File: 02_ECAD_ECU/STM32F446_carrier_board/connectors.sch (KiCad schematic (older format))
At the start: 2 parts, among them J1 FX10A-168S-SV, J2 FX10A-168P-SV_(71)

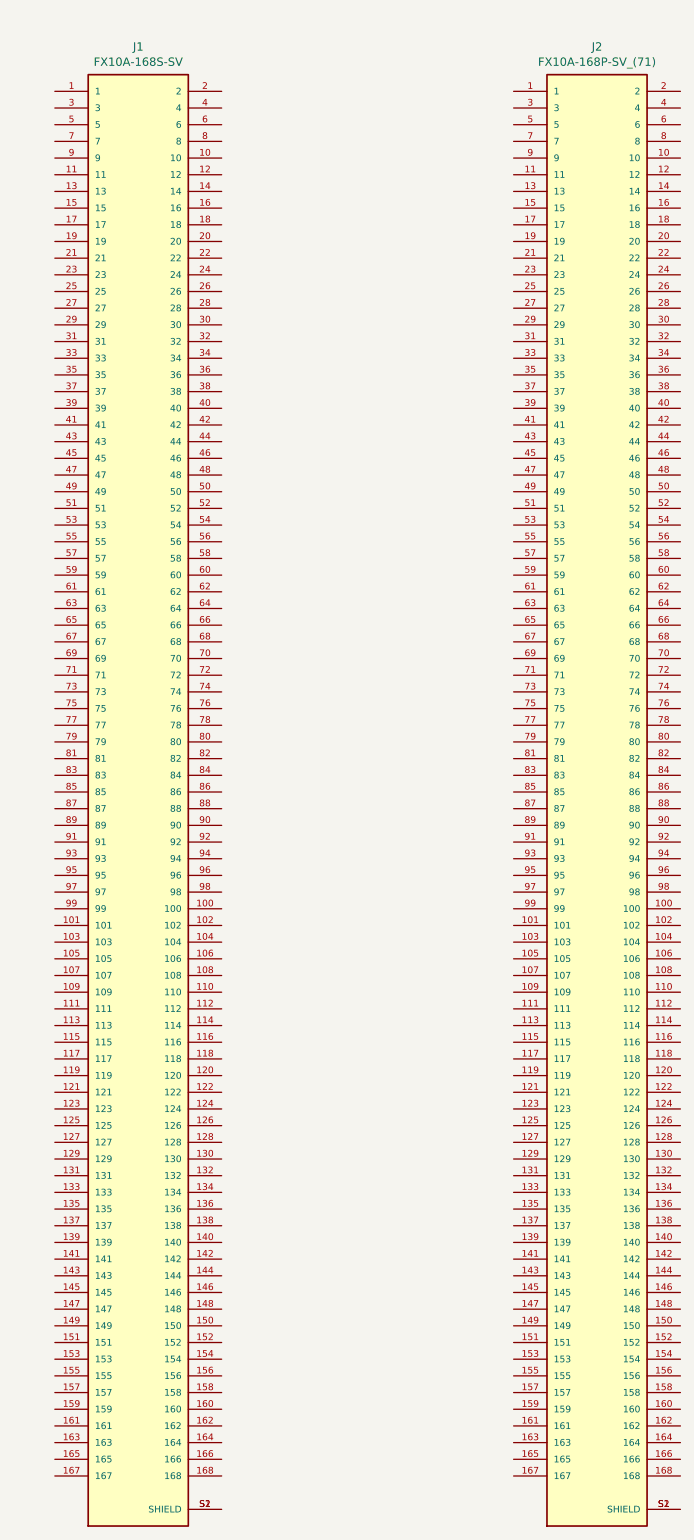
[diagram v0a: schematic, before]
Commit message: added connectors to ecad project
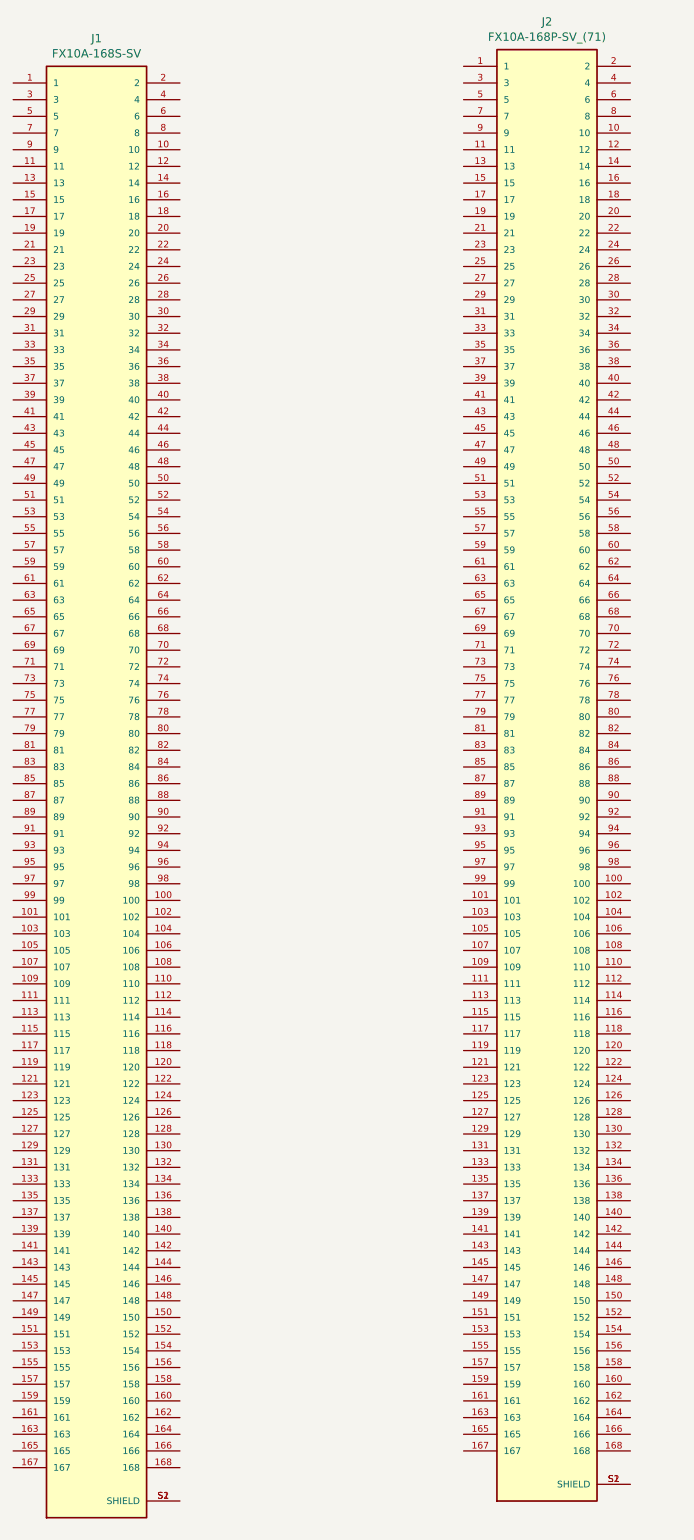
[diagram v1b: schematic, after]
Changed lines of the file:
@@
 $EndDescr
 $Comp
-L max_KiCAD_lib:FX10A-168P-SV_(71) J?
-U 1 1 614A8335
-P 4850 5600
-AR Path="/614A8335" Ref="J?"  Part="1"
-AR Path="/614A3ED5/614A8335" Ref="J2"  Part="1"
-F 0 "J2" H 4850 10167 50  0000 C CNN
-F 1 "FX10A-168P-SV_(71)" H 4850 10076 50  0000 C CNN
-F 2 "max_KiCAD_lib:HRS_FX10A-168P-SV" H 4850 5600 50  0001 L BNN
-F 3 "" H 4850 5600 50  0001 L BNN
-F 4 "HRS" H 4850 5600 50  0001 L BNN "MANUFACTURER"
-F 5 "Manufacturer Recommendation" H 4850 5600 50  0001 L BNN "STANDARD"
-	1    4850 5600
+L max_KiCAD_lib:FX10A-168P-SV_(71) J2
+U 1 1 6143D95B
+P 4550 5450
+F 0 "J2" H 4550 10017 50  0000 C CNN
+F 1 "FX10A-168P-SV_(71)" H 4550 9926 50  0000 C CNN
+F 2 "max_KiCAD_lib:HRS_FX10A-168P-SV" H 4550 5450 50  0001 L BNN
+F 3 "" H 4550 5450 50  0001 L BNN
+F 4 "HRS" H 4550 5450 50  0001 L BNN "MANUFACTURER"
+F 5 "Manufacturer Recommendation" H 4550 5450 50  0001 L BNN "STANDARD"
+	1    4550 5450
 	1    0    0    -1
 $EndComp
 $Comp
-L max_KiCAD_lib:FX10A-168S-SV J?
-U 1 1 614A833D
-P 2100 5600
-AR Path="/614A833D" Ref="J?"  Part="1"
-AR Path="/614A3ED5/614A833D" Ref="J1"  Part="1"
-F 0 "J1" H 2100 10167 50  0000 C CNN
-F 1 "FX10A-168S-SV" H 2100 10076 50  0000 C CNN
-F 2 "max_KiCAD_lib:HRS_FX10A-168S-SV" H 2100 5600 50  0001 L BNN
-F 3 "" H 2100 5600 50  0001 L BNN
-F 4 "HRS" H 2100 5600 50  0001 L BNN "MANUFACTURER"
-F 5 "Manufacturer Recommendation" H 2100 5600 50  0001 L BNN "STANDARD"
-	1    2100 5600
+L max_KiCAD_lib:FX10A-168S-SV J1
+U 1 1 61442947
+P 1850 5550
+F 0 "J1" H 1850 10117 50  0000 C CNN
+F 1 "FX10A-168S-SV" H 1850 10026 50  0000 C CNN
+F 2 "max_KiCAD_lib:HRS_FX10A-168S-SV" H 1850 5550 50  0001 L BNN
+F 3 "" H 1850 5550 50  0001 L BNN
+F 4 "HRS" H 1850 5550 50  0001 L BNN "MANUFACTURER"
+F 5 "Manufacturer Recommendation" H 1850 5550 50  0001 L BNN "STANDARD"
+	1    1850 5550
 	1    0    0    -1
 $EndComp
